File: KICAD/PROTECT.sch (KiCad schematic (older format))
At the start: 13 parts

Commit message: review w/ jmt
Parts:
- R55: renamed from R?; footprint Resistor_SMD:R_0805_2012Metric -> (none)
- R56, R57, R58: renamed from R?; footprint Resistor_SMD:R_0805_2012Metric_Pad1.15x1.40mm_HandSolder -> (none)
- gave numbers to parts that had none: 9
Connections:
- net labels added: GND
- net labels removed: GNDPWR
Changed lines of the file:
@@
 $Descr A4 11693 8268
 encoding utf-8
-Sheet 10 17
+Sheet 9 17
 Title ""
 Date ""
@@
 VProt
 $Comp
-L Device:Q_PMOS_GDS Q?
+L Device:Q_PMOS_GDS Q9
 U 1 1 610FCCAA
 P 4250 2950
-AR Path="/614794AE/610FCCAA" Ref="Q?"  Part="1"
-AR Path="/61456C6A/610FCCAA" Ref="Q?"  Part="1"
+AR Path="/614794AE/610FCCAA" Ref="Q9"  Part="1"
+AR Path="/61456C6A/610FCCAA" Ref="Q6"  Part="1"
 AR Path="/618D2416/610FCCAA" Ref="Q?"  Part="1"
-F 0 "Q?" V 4592 2950 50  0000 C CNN
+F 0 "Q6" V 4592 2950 50  0000 C CNN
 F 1 "SQM120" V 4501 2950 50  0000 C CNN
 F 2 "Package_TO_SOT_SMD:TO-263-2" H 4450 3050 50  0001 C CNN
@@
 $EndComp
 $Comp
-L Device:Q_PMOS_GDS Q?
+L Device:Q_PMOS_GDS Q11
 U 1 1 610FED91
 P 7800 2950
-AR Path="/614794AE/610FED91" Ref="Q?"  Part="1"
-AR Path="/61456C6A/610FED91" Ref="Q?"  Part="1"
+AR Path="/614794AE/610FED91" Ref="Q11"  Part="1"
+AR Path="/61456C6A/610FED91" Ref="Q8"  Part="1"
 AR Path="/618D2416/610FED91" Ref="Q?"  Part="1"
-F 0 "Q?" V 8142 2950 50  0000 C CNN
+F 0 "Q8" V 8142 2950 50  0000 C CNN
 F 1 "SQM120" V 8051 2950 50  0000 C CNN
 F 2 "Package_TO_SOT_SMD:TO-263-2" H 8000 3050 50  0001 C CNN
@@
 $EndComp
 $Comp
-L Device:D_Zener D?
+L Device:D_Zener D5
 U 1 1 61100A0F
 P 4550 3100
-AR Path="/614794AE/61100A0F" Ref="D?"  Part="1"
-AR Path="/61456C6A/61100A0F" Ref="D?"  Part="1"
+AR Path="/614794AE/61100A0F" Ref="D5"  Part="1"
+AR Path="/61456C6A/61100A0F" Ref="D2"  Part="1"
 AR Path="/618D2416/61100A0F" Ref="D?"  Part="1"
-F 0 "D?" V 4504 3180 50  0000 L CNN
+F 0 "D2" V 4504 3180 50  0000 L CNN
 F 1 "MMSZ5245" V 4595 3180 50  0000 L CNN
 F 2 "Diode_SMD:D_SOD-123" H 4550 3100 50  0001 C CNN
@@
 $EndComp
 $Comp
-L Device:R R?
+L Device:R R55
 U 1 1 61102FC8
 P 4250 3700
-AR Path="/614794AE/61102FC8" Ref="R?"  Part="1"
-AR Path="/61456C6A/61102FC8" Ref="R?"  Part="1"
+AR Path="/614794AE/61102FC8" Ref="R55"  Part="1"
+AR Path="/61456C6A/61102FC8" Ref="R51"  Part="1"
 AR Path="/618D2416/61102FC8" Ref="R?"  Part="1"
-F 0 "R?" H 4320 3746 50  0000 L CNN
+F 0 "R51" H 4320 3746 50  0000 L CNN
 F 1 "330k" H 4320 3655 50  0000 L CNN
-F 2 "Resistor_SMD:R_0805_2012Metric" V 4180 3700 50  0001 C CNN
+F 2 "" V 4180 3700 50  0001 C CNN
 F 3 "~" H 4250 3700 50  0001 C CNN
 	1    4250 3700
@@
 	4250 3550 4250 3350
 Connection ~ 4250 3350
-$Comp
-L power:GNDPWR #PWR0121
-U 1 1 61104B6E
-P 4250 4050
-AR Path="/614794AE/61104B6E" Ref="#PWR0121"  Part="1"
-AR Path="/61456C6A/61104B6E" Ref="#PWR0124"  Part="1"
-AR Path="/618D2416/61104B6E" Ref="#PWR?"  Part="1"
-F 0 "#PWR?" H 4250 3850 50  0001 C CNN
-F 1 "GNDPWR" H 4254 3896 50  0000 C CNN
-F 2 "" H 4250 4000 50  0001 C CNN
-F 3 "" H 4250 4000 50  0001 C CNN
-	1    4250 4050
-	1    0    0    -1
-$EndComp
 Wire Wire Line
 	4250 4050 4250 3850
@@
 	3900 2500 5100 2500
 $Comp
-L Transistor_BJT:BC857 Q?
+L Transistor_BJT:BC857 Q10
 U 1 1 6110710F
 P 6600 3300
-AR Path="/614794AE/6110710F" Ref="Q?"  Part="1"
-AR Path="/61456C6A/6110710F" Ref="Q?"  Part="1"
+AR Path="/614794AE/6110710F" Ref="Q10"  Part="1"
+AR Path="/61456C6A/6110710F" Ref="Q7"  Part="1"
 AR Path="/618D2416/6110710F" Ref="Q?"  Part="1"
-F 0 "Q?" H 6791 3346 50  0000 L CNN
+F 0 "Q7" H 6791 3346 50  0000 L CNN
 F 1 "BC857" H 6791 3255 50  0000 L CNN
 F 2 "Package_TO_SOT_SMD:SOT-23" H 6800 3225 50  0001 L CIN
@@
 $EndComp
 $Comp
-L Device:D_Zener D?
+L Device:D_Zener D7
 U 1 1 61107DEE
 P 7250 3200
-AR Path="/614794AE/61107DEE" Ref="D?"  Part="1"
-AR Path="/61456C6A/61107DEE" Ref="D?"  Part="1"
+AR Path="/614794AE/61107DEE" Ref="D7"  Part="1"
+AR Path="/61456C6A/61107DEE" Ref="D4"  Part="1"
 AR Path="/618D2416/61107DEE" Ref="D?"  Part="1"
-F 0 "D?" V 7204 3280 50  0000 L CNN
+F 0 "D4" V 7204 3280 50  0000 L CNN
 F 1 "MMSZ5245" V 7295 3280 50  0000 L CNN
 F 2 "Diode_SMD:D_SOD-123" H 7250 3200 50  0001 C CNN
@@
 $EndComp
 $Comp
-L Device:R R?
+L Device:R R56
 U 1 1 611083FB
 P 5900 3100
-AR Path="/614794AE/611083FB" Ref="R?"  Part="1"
-AR Path="/61456C6A/611083FB" Ref="R?"  Part="1"
+AR Path="/614794AE/611083FB" Ref="R56"  Part="1"
+AR Path="/61456C6A/611083FB" Ref="R52"  Part="1"
 AR Path="/618D2416/611083FB" Ref="R?"  Part="1"
-F 0 "R?" H 5970 3146 50  0000 L CNN
+F 0 "R52" H 5970 3146 50  0000 L CNN
 F 1 "100k" H 5970 3055 50  0000 L CNN
-F 2 "Resistor_SMD:R_0805_2012Metric_Pad1.15x1.40mm_HandSolder" V 5830 3100 50  0001 C CNN
+F 2 "" V 5830 3100 50  0001 C CNN
 F 3 "~" H 5900 3100 50  0001 C CNN
 	1    5900 3100
@@
 	5900 2950 5900 2850
 $Comp
-L Device:R R?
+L Device:R R57
 U 1 1 6110B925
 P 6250 3300
-AR Path="/614794AE/6110B925" Ref="R?"  Part="1"
-AR Path="/61456C6A/6110B925" Ref="R?"  Part="1"
+AR Path="/614794AE/6110B925" Ref="R57"  Part="1"
+AR Path="/61456C6A/6110B925" Ref="R53"  Part="1"
 AR Path="/618D2416/6110B925" Ref="R?"  Part="1"
-F 0 "R?" V 6043 3300 50  0000 C CNN
+F 0 "R53" V 6043 3300 50  0000 C CNN
 F 1 "100k" V 6134 3300 50  0000 C CNN
-F 2 "Resistor_SMD:R_0805_2012Metric_Pad1.15x1.40mm_HandSolder" V 6180 3300 50  0001 C CNN
+F 2 "" V 6180 3300 50  0001 C CNN
 F 3 "~" H 6250 3300 50  0001 C CNN
 	1    6250 3300
@@
 Connection ~ 7250 2850
 $Comp
-L Device:R R?
+L Device:R R58
 U 1 1 61115761
 P 7800 3850
-AR Path="/614794AE/61115761" Ref="R?"  Part="1"
-AR Path="/61456C6A/61115761" Ref="R?"  Part="1"
+AR Path="/614794AE/61115761" Ref="R58"  Part="1"
+AR Path="/61456C6A/61115761" Ref="R54"  Part="1"
 AR Path="/618D2416/61115761" Ref="R?"  Part="1"
-F 0 "R?" H 7870 3896 50  0000 L CNN
+F 0 "R54" H 7870 3896 50  0000 L CNN
 F 1 "1M" H 7870 3805 50  0000 L CNN
-F 2 "Resistor_SMD:R_0805_2012Metric_Pad1.15x1.40mm_HandSolder" V 7730 3850 50  0001 C CNN
+F 2 "" V 7730 3850 50  0001 C CNN
 F 3 "~" H 7800 3850 50  0001 C CNN
 	1    7800 3850
-	1    0    0    -1
-$EndComp
-$Comp
-L power:GNDPWR #PWR0122
-U 1 1 6111576B
-P 7800 4050
-AR Path="/614794AE/6111576B" Ref="#PWR0122"  Part="1"
-AR Path="/61456C6A/6111576B" Ref="#PWR0125"  Part="1"
-AR Path="/618D2416/6111576B" Ref="#PWR?"  Part="1"
-F 0 "#PWR?" H 7800 3850 50  0001 C CNN
-F 1 "GNDPWR" H 7804 3896 50  0000 C CNN
-F 2 "" H 7800 4000 50  0001 C CNN
-F 3 "" H 7800 4000 50  0001 C CNN
-	1    7800 4050
 	1    0    0    -1
 $EndComp
@@
 Wire Wire Line
 	5900 3850 5900 4050
-$Comp
-L power:GNDPWR #PWR0123
-U 1 1 611168C4
-P 5900 4050
-AR Path="/614794AE/611168C4" Ref="#PWR0123"  Part="1"
-AR Path="/61456C6A/611168C4" Ref="#PWR0126"  Part="1"
-AR Path="/618D2416/611168C4" Ref="#PWR?"  Part="1"
-F 0 "#PWR?" H 5900 3850 50  0001 C CNN
-F 1 "GNDPWR" H 5904 3896 50  0000 C CNN
-F 2 "" H 5900 4000 50  0001 C CNN
-F 3 "" H 5900 4000 50  0001 C CNN
-	1    5900 4050
-	1    0    0    -1
-$EndComp
 Wire Wire Line
 	5900 3300 5900 3550
 $Comp
-L Device:D_Zener D?
+L Device:D_Zener D6
 U 1 1 61107C25
 P 5900 3700
-AR Path="/614794AE/61107C25" Ref="D?"  Part="1"
-AR Path="/61456C6A/61107C25" Ref="D?"  Part="1"
+AR Path="/614794AE/61107C25" Ref="D6"  Part="1"
+AR Path="/61456C6A/61107C25" Ref="D3"  Part="1"
 AR Path="/618D2416/61107C25" Ref="D?"  Part="1"
-F 0 "D?" V 5854 3780 50  0000 L CNN
+F 0 "D3" V 5854 3780 50  0000 L CNN
 F 1 "MMSZ5262" V 5945 3780 50  0000 L CNN
 F 2 "Diode_SMD:D_SOD-123" H 5900 3700 50  0001 C CNN
@@
 $EndComp
 $Comp
-L Connector:TestPoint TP?
+L Connector:TestPoint TP27
 U 1 1 612D3587
 P 5350 2850
-AR Path="/614794AE/612D3587" Ref="TP?"  Part="1"
-AR Path="/61456C6A/612D3587" Ref="TP?"  Part="1"
+AR Path="/614794AE/612D3587" Ref="TP27"  Part="1"
+AR Path="/61456C6A/612D3587" Ref="TP24"  Part="1"
 AR Path="/618D2416/612D3587" Ref="TP?"  Part="1"
-F 0 "TP?" H 5300 3100 50  0000 L CNN
+F 0 "TP24" H 5300 3100 50  0000 L CNN
 F 1 "TP_POP" H 5350 2750 50  0000 C CNN
 F 2 "" H 5550 2850 50  0001 C CNN
@@
 	5350 2850 5900 2850
 $Comp
-L Connector:TestPoint TP?
+L Connector:TestPoint TP28
 U 1 1 612DA888
 P 8400 2850
-AR Path="/614794AE/612DA888" Ref="TP?"  Part="1"
-AR Path="/61456C6A/612DA888" Ref="TP?"  Part="1"
+AR Path="/614794AE/612DA888" Ref="TP28"  Part="1"
+AR Path="/61456C6A/612DA888" Ref="TP25"  Part="1"
 AR Path="/618D2416/612DA888" Ref="TP?"  Part="1"
-F 0 "TP?" H 8350 3100 50  0000 L CNN
+F 0 "TP25" H 8350 3100 50  0000 L CNN
 F 1 "TP_POP" H 8400 2750 50  0000 C CNN
 F 2 "" H 8600 2850 50  0001 C CNN
@@
 	8000 2850 8400 2850
 $Comp
-L Connector:TestPoint TP?
+L Connector:TestPoint TP26
 U 1 1 614EA2DB
 P 3650 2850
-AR Path="/614794AE/614EA2DB" Ref="TP?"  Part="1"
-AR Path="/61456C6A/614EA2DB" Ref="TP?"  Part="1"
+AR Path="/614794AE/614EA2DB" Ref="TP26"  Part="1"
+AR Path="/61456C6A/614EA2DB" Ref="TP23"  Part="1"
 AR Path="/618D2416/614EA2DB" Ref="TP?"  Part="1"
-F 0 "TP?" H 3600 3100 50  0000 L CNN
+F 0 "TP23" H 3600 3100 50  0000 L CNN
 F 1 "TP_POP" H 3650 2750 50  0000 C CNN
 F 2 "" H 3850 2850 50  0001 C CNN
@@
 Wire Wire Line
 	3650 2850 4050 2850
+$Comp
+L power:GND #PWR069
+U 1 1 61BA1370
+P 4250 4050
+AR Path="/61456C6A/61BA1370" Ref="#PWR069"  Part="1"
+AR Path="/614794AE/61BA1370" Ref="#PWR072"  Part="1"
+F 0 "#PWR069" H 4250 3800 50  0001 C CNN
+F 1 "GND" H 4255 3877 50  0000 C CNN
+F 2 "" H 4250 4050 50  0001 C CNN
+F 3 "" H 4250 4050 50  0001 C CNN
+	1    4250 4050
+	1    0    0    -1
+$EndComp
+$Comp
+L power:GND #PWR070
+U 1 1 61BA1902
+P 5900 4050
+AR Path="/61456C6A/61BA1902" Ref="#PWR070"  Part="1"
+AR Path="/614794AE/61BA1902" Ref="#PWR073"  Part="1"
+F 0 "#PWR070" H 5900 3800 50  0001 C CNN
+F 1 "GND" H 5905 3877 50  0000 C CNN
+F 2 "" H 5900 4050 50  0001 C CNN
+F 3 "" H 5900 4050 50  0001 C CNN
+	1    5900 4050
+	1    0    0    -1
+$EndComp
+$Comp
+L power:GND #PWR071
+U 1 1 61BA1F25
+P 7800 4050
+AR Path="/61456C6A/61BA1F25" Ref="#PWR071"  Part="1"
+AR Path="/614794AE/61BA1F25" Ref="#PWR074"  Part="1"
+F 0 "#PWR071" H 7800 3800 50  0001 C CNN
+F 1 "GND" H 7805 3877 50  0000 C CNN
+F 2 "" H 7800 4050 50  0001 C CNN
+F 3 "" H 7800 4050 50  0001 C CNN
+	1    7800 4050
+	1    0    0    -1
+$EndComp
 $EndSCHEMATC

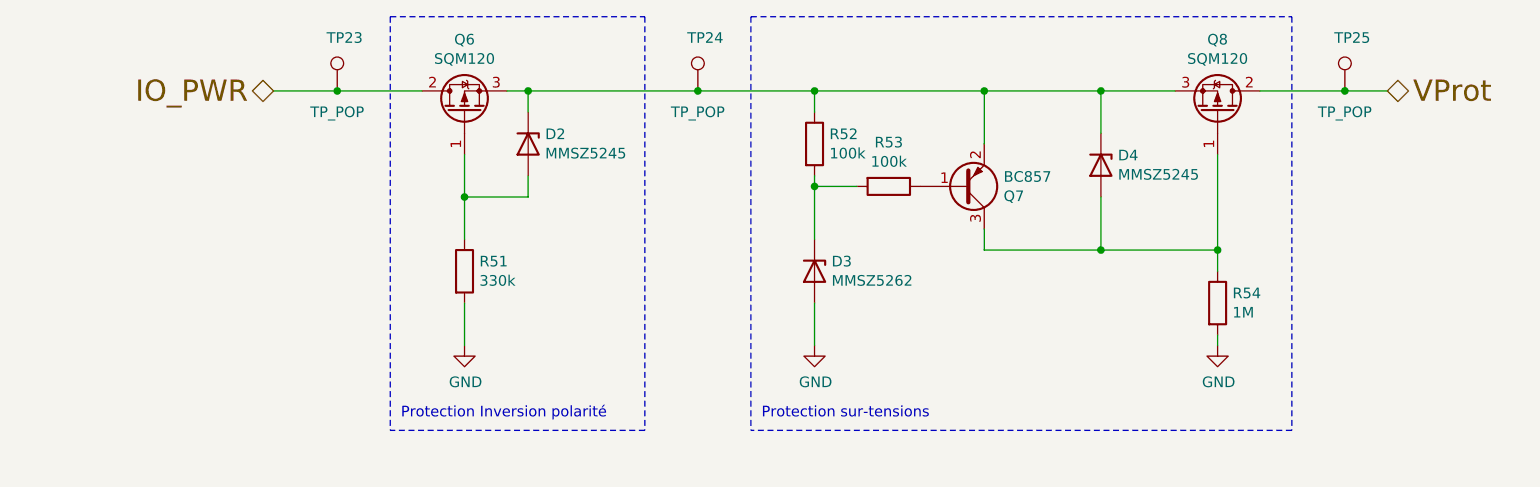
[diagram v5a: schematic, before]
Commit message: edit footprints by jmt
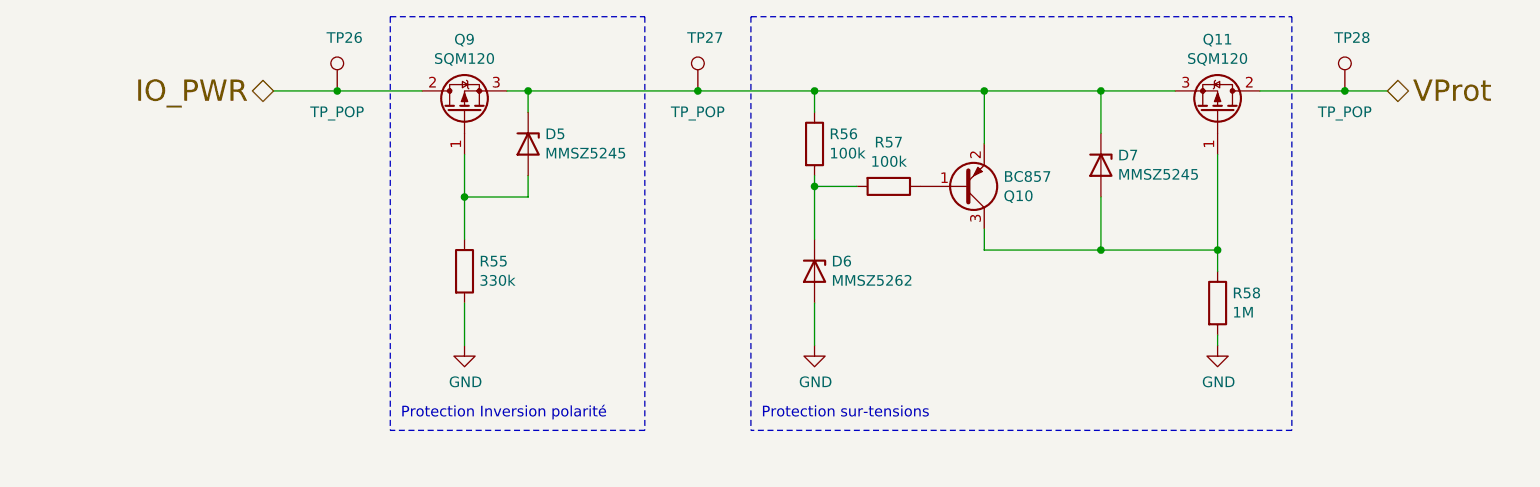
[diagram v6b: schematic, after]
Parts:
- R55, R56, R57, R58: footprint (none) -> Resistor_SMD:R_0805_2012Metric_Pad1.15x1.40mm_HandSolder
- TP26, TP27, TP28: footprint (none) -> TestPoint:TestPoint_Loop_D1.80mm_Drill1.0mm_Beaded
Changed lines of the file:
@@
 AR Path="/61456C6A/610FCCAA" Ref="Q6"  Part="1"
 AR Path="/618D2416/610FCCAA" Ref="Q?"  Part="1"
-F 0 "Q6" V 4592 2950 50  0000 C CNN
+F 0 "Q9" V 4592 2950 50  0000 C CNN
 F 1 "SQM120" V 4501 2950 50  0000 C CNN
 F 2 "Package_TO_SOT_SMD:TO-263-2" H 4450 3050 50  0001 C CNN
@@
 AR Path="/61456C6A/610FED91" Ref="Q8"  Part="1"
 AR Path="/618D2416/610FED91" Ref="Q?"  Part="1"
-F 0 "Q8" V 8142 2950 50  0000 C CNN
+F 0 "Q11" V 8142 2950 50  0000 C CNN
 F 1 "SQM120" V 8051 2950 50  0000 C CNN
 F 2 "Package_TO_SOT_SMD:TO-263-2" H 8000 3050 50  0001 C CNN
@@
 AR Path="/61456C6A/61100A0F" Ref="D2"  Part="1"
 AR Path="/618D2416/61100A0F" Ref="D?"  Part="1"
-F 0 "D2" V 4504 3180 50  0000 L CNN
+F 0 "D5" V 4504 3180 50  0000 L CNN
 F 1 "MMSZ5245" V 4595 3180 50  0000 L CNN
 F 2 "Diode_SMD:D_SOD-123" H 4550 3100 50  0001 C CNN
@@
 AR Path="/61456C6A/61102FC8" Ref="R51"  Part="1"
 AR Path="/618D2416/61102FC8" Ref="R?"  Part="1"
-F 0 "R51" H 4320 3746 50  0000 L CNN
+F 0 "R55" H 4320 3746 50  0000 L CNN
 F 1 "330k" H 4320 3655 50  0000 L CNN
-F 2 "" V 4180 3700 50  0001 C CNN
+F 2 "Resistor_SMD:R_0805_2012Metric_Pad1.15x1.40mm_HandSolder" V 4180 3700 50  0001 C CNN
 F 3 "~" H 4250 3700 50  0001 C CNN
 	1    4250 3700
@@
 AR Path="/61456C6A/6110710F" Ref="Q7"  Part="1"
 AR Path="/618D2416/6110710F" Ref="Q?"  Part="1"
-F 0 "Q7" H 6791 3346 50  0000 L CNN
+F 0 "Q10" H 6791 3346 50  0000 L CNN
 F 1 "BC857" H 6791 3255 50  0000 L CNN
 F 2 "Package_TO_SOT_SMD:SOT-23" H 6800 3225 50  0001 L CIN
@@
 AR Path="/61456C6A/61107DEE" Ref="D4"  Part="1"
 AR Path="/618D2416/61107DEE" Ref="D?"  Part="1"
-F 0 "D4" V 7204 3280 50  0000 L CNN
+F 0 "D7" V 7204 3280 50  0000 L CNN
 F 1 "MMSZ5245" V 7295 3280 50  0000 L CNN
 F 2 "Diode_SMD:D_SOD-123" H 7250 3200 50  0001 C CNN
@@
 AR Path="/61456C6A/611083FB" Ref="R52"  Part="1"
 AR Path="/618D2416/611083FB" Ref="R?"  Part="1"
-F 0 "R52" H 5970 3146 50  0000 L CNN
+F 0 "R56" H 5970 3146 50  0000 L CNN
 F 1 "100k" H 5970 3055 50  0000 L CNN
-F 2 "" V 5830 3100 50  0001 C CNN
+F 2 "Resistor_SMD:R_0805_2012Metric_Pad1.15x1.40mm_HandSolder" V 5830 3100 50  0001 C CNN
 F 3 "~" H 5900 3100 50  0001 C CNN
 	1    5900 3100
@@
 AR Path="/61456C6A/6110B925" Ref="R53"  Part="1"
 AR Path="/618D2416/6110B925" Ref="R?"  Part="1"
-F 0 "R53" V 6043 3300 50  0000 C CNN
+F 0 "R57" V 6043 3300 50  0000 C CNN
 F 1 "100k" V 6134 3300 50  0000 C CNN
-F 2 "" V 6180 3300 50  0001 C CNN
+F 2 "Resistor_SMD:R_0805_2012Metric_Pad1.15x1.40mm_HandSolder" V 6180 3300 50  0001 C CNN
 F 3 "~" H 6250 3300 50  0001 C CNN
 	1    6250 3300
@@
 AR Path="/61456C6A/61115761" Ref="R54"  Part="1"
 AR Path="/618D2416/61115761" Ref="R?"  Part="1"
-F 0 "R54" H 7870 3896 50  0000 L CNN
+F 0 "R58" H 7870 3896 50  0000 L CNN
 F 1 "1M" H 7870 3805 50  0000 L CNN
-F 2 "" V 7730 3850 50  0001 C CNN
+F 2 "Resistor_SMD:R_0805_2012Metric_Pad1.15x1.40mm_HandSolder" V 7730 3850 50  0001 C CNN
 F 3 "~" H 7800 3850 50  0001 C CNN
 	1    7800 3850
@@
 AR Path="/61456C6A/61107C25" Ref="D3"  Part="1"
 AR Path="/618D2416/61107C25" Ref="D?"  Part="1"
-F 0 "D3" V 5854 3780 50  0000 L CNN
+F 0 "D6" V 5854 3780 50  0000 L CNN
 F 1 "MMSZ5262" V 5945 3780 50  0000 L CNN
 F 2 "Diode_SMD:D_SOD-123" H 5900 3700 50  0001 C CNN
@@
 AR Path="/61456C6A/612D3587" Ref="TP24"  Part="1"
 AR Path="/618D2416/612D3587" Ref="TP?"  Part="1"
-F 0 "TP24" H 5300 3100 50  0000 L CNN
+F 0 "TP27" H 5300 3100 50  0000 L CNN
 F 1 "TP_POP" H 5350 2750 50  0000 C CNN
-F 2 "" H 5550 2850 50  0001 C CNN
+F 2 "TestPoint:TestPoint_Loop_D1.80mm_Drill1.0mm_Beaded" H 5550 2850 50  0001 C CNN
 F 3 "~" H 5550 2850 50  0001 C CNN
 	1    5350 2850
@@
 AR Path="/61456C6A/612DA888" Ref="TP25"  Part="1"
 AR Path="/618D2416/612DA888" Ref="TP?"  Part="1"
-F 0 "TP25" H 8350 3100 50  0000 L CNN
+F 0 "TP28" H 8350 3100 50  0000 L CNN
 F 1 "TP_POP" H 8400 2750 50  0000 C CNN
-F 2 "" H 8600 2850 50  0001 C CNN
+F 2 "TestPoint:TestPoint_Loop_D1.80mm_Drill1.0mm_Beaded" H 8600 2850 50  0001 C CNN
 F 3 "~" H 8600 2850 50  0001 C CNN
 	1    8400 2850
@@
 AR Path="/61456C6A/614EA2DB" Ref="TP23"  Part="1"
 AR Path="/618D2416/614EA2DB" Ref="TP?"  Part="1"
-F 0 "TP23" H 3600 3100 50  0000 L CNN
+F 0 "TP26" H 3600 3100 50  0000 L CNN
 F 1 "TP_POP" H 3650 2750 50  0000 C CNN
-F 2 "" H 3850 2850 50  0001 C CNN
+F 2 "TestPoint:TestPoint_Loop_D1.80mm_Drill1.0mm_Beaded" H 3850 2850 50  0001 C CNN
 F 3 "~" H 3850 2850 50  0001 C CNN
 	1    3650 2850
@@
 AR Path="/61456C6A/61BA1370" Ref="#PWR069"  Part="1"
 AR Path="/614794AE/61BA1370" Ref="#PWR072"  Part="1"
-F 0 "#PWR069" H 4250 3800 50  0001 C CNN
+F 0 "#PWR072" H 4250 3800 50  0001 C CNN
 F 1 "GND" H 4255 3877 50  0000 C CNN
 F 2 "" H 4250 4050 50  0001 C CNN
@@
 AR Path="/61456C6A/61BA1902" Ref="#PWR070"  Part="1"
 AR Path="/614794AE/61BA1902" Ref="#PWR073"  Part="1"
-F 0 "#PWR070" H 5900 3800 50  0001 C CNN
+F 0 "#PWR073" H 5900 3800 50  0001 C CNN
 F 1 "GND" H 5905 3877 50  0000 C CNN
 F 2 "" H 5900 4050 50  0001 C CNN
@@
 AR Path="/61456C6A/61BA1F25" Ref="#PWR071"  Part="1"
 AR Path="/614794AE/61BA1F25" Ref="#PWR074"  Part="1"
-F 0 "#PWR071" H 7800 3800 50  0001 C CNN
+F 0 "#PWR074" H 7800 3800 50  0001 C CNN
 F 1 "GND" H 7805 3877 50  0000 C CNN
 F 2 "" H 7800 4050 50  0001 C CNN

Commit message: route + work on djd
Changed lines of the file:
@@
 AR Path="/61456C6A/610FCCAA" Ref="Q6"  Part="1"
 AR Path="/618D2416/610FCCAA" Ref="Q?"  Part="1"
-F 0 "Q9" V 4592 2950 50  0000 C CNN
+F 0 "Q6" V 4592 2950 50  0000 C CNN
 F 1 "SQM120" V 4501 2950 50  0000 C CNN
 F 2 "Package_TO_SOT_SMD:TO-263-2" H 4450 3050 50  0001 C CNN
@@
 AR Path="/61456C6A/610FED91" Ref="Q8"  Part="1"
 AR Path="/618D2416/610FED91" Ref="Q?"  Part="1"
-F 0 "Q11" V 8142 2950 50  0000 C CNN
+F 0 "Q8" V 8142 2950 50  0000 C CNN
 F 1 "SQM120" V 8051 2950 50  0000 C CNN
 F 2 "Package_TO_SOT_SMD:TO-263-2" H 8000 3050 50  0001 C CNN
@@
 AR Path="/61456C6A/61100A0F" Ref="D2"  Part="1"
 AR Path="/618D2416/61100A0F" Ref="D?"  Part="1"
-F 0 "D5" V 4504 3180 50  0000 L CNN
+F 0 "D2" V 4504 3180 50  0000 L CNN
 F 1 "MMSZ5245" V 4595 3180 50  0000 L CNN
 F 2 "Diode_SMD:D_SOD-123" H 4550 3100 50  0001 C CNN
@@
 AR Path="/61456C6A/61102FC8" Ref="R51"  Part="1"
 AR Path="/618D2416/61102FC8" Ref="R?"  Part="1"
-F 0 "R55" H 4320 3746 50  0000 L CNN
+F 0 "R51" H 4320 3746 50  0000 L CNN
 F 1 "330k" H 4320 3655 50  0000 L CNN
 F 2 "Resistor_SMD:R_0805_2012Metric_Pad1.15x1.40mm_HandSolder" V 4180 3700 50  0001 C CNN
@@
 AR Path="/61456C6A/6110710F" Ref="Q7"  Part="1"
 AR Path="/618D2416/6110710F" Ref="Q?"  Part="1"
-F 0 "Q10" H 6791 3346 50  0000 L CNN
+F 0 "Q7" H 6791 3346 50  0000 L CNN
 F 1 "BC857" H 6791 3255 50  0000 L CNN
 F 2 "Package_TO_SOT_SMD:SOT-23" H 6800 3225 50  0001 L CIN
@@
 AR Path="/61456C6A/61107DEE" Ref="D4"  Part="1"
 AR Path="/618D2416/61107DEE" Ref="D?"  Part="1"
-F 0 "D7" V 7204 3280 50  0000 L CNN
+F 0 "D4" V 7204 3280 50  0000 L CNN
 F 1 "MMSZ5245" V 7295 3280 50  0000 L CNN
 F 2 "Diode_SMD:D_SOD-123" H 7250 3200 50  0001 C CNN
@@
 AR Path="/61456C6A/611083FB" Ref="R52"  Part="1"
 AR Path="/618D2416/611083FB" Ref="R?"  Part="1"
-F 0 "R56" H 5970 3146 50  0000 L CNN
+F 0 "R52" H 5970 3146 50  0000 L CNN
 F 1 "100k" H 5970 3055 50  0000 L CNN
 F 2 "Resistor_SMD:R_0805_2012Metric_Pad1.15x1.40mm_HandSolder" V 5830 3100 50  0001 C CNN
@@
 AR Path="/61456C6A/6110B925" Ref="R53"  Part="1"
 AR Path="/618D2416/6110B925" Ref="R?"  Part="1"
-F 0 "R57" V 6043 3300 50  0000 C CNN
+F 0 "R53" V 6043 3300 50  0000 C CNN
 F 1 "100k" V 6134 3300 50  0000 C CNN
 F 2 "Resistor_SMD:R_0805_2012Metric_Pad1.15x1.40mm_HandSolder" V 6180 3300 50  0001 C CNN
@@
 AR Path="/61456C6A/61115761" Ref="R54"  Part="1"
 AR Path="/618D2416/61115761" Ref="R?"  Part="1"
-F 0 "R58" H 7870 3896 50  0000 L CNN
+F 0 "R54" H 7870 3896 50  0000 L CNN
 F 1 "1M" H 7870 3805 50  0000 L CNN
 F 2 "Resistor_SMD:R_0805_2012Metric_Pad1.15x1.40mm_HandSolder" V 7730 3850 50  0001 C CNN
@@
 AR Path="/61456C6A/61107C25" Ref="D3"  Part="1"
 AR Path="/618D2416/61107C25" Ref="D?"  Part="1"
-F 0 "D6" V 5854 3780 50  0000 L CNN
+F 0 "D3" V 5854 3780 50  0000 L CNN
 F 1 "MMSZ5262" V 5945 3780 50  0000 L CNN
 F 2 "Diode_SMD:D_SOD-123" H 5900 3700 50  0001 C CNN
@@
 AR Path="/61456C6A/612D3587" Ref="TP24"  Part="1"
 AR Path="/618D2416/612D3587" Ref="TP?"  Part="1"
-F 0 "TP27" H 5300 3100 50  0000 L CNN
+F 0 "TP24" H 5300 3100 50  0000 L CNN
 F 1 "TP_POP" H 5350 2750 50  0000 C CNN
 F 2 "TestPoint:TestPoint_Loop_D1.80mm_Drill1.0mm_Beaded" H 5550 2850 50  0001 C CNN
@@
 AR Path="/61456C6A/612DA888" Ref="TP25"  Part="1"
 AR Path="/618D2416/612DA888" Ref="TP?"  Part="1"
-F 0 "TP28" H 8350 3100 50  0000 L CNN
+F 0 "TP25" H 8350 3100 50  0000 L CNN
 F 1 "TP_POP" H 8400 2750 50  0000 C CNN
 F 2 "TestPoint:TestPoint_Loop_D1.80mm_Drill1.0mm_Beaded" H 8600 2850 50  0001 C CNN
@@
 AR Path="/61456C6A/614EA2DB" Ref="TP23"  Part="1"
 AR Path="/618D2416/614EA2DB" Ref="TP?"  Part="1"
-F 0 "TP26" H 3600 3100 50  0000 L CNN
+F 0 "TP23" H 3600 3100 50  0000 L CNN
 F 1 "TP_POP" H 3650 2750 50  0000 C CNN
 F 2 "TestPoint:TestPoint_Loop_D1.80mm_Drill1.0mm_Beaded" H 3850 2850 50  0001 C CNN
